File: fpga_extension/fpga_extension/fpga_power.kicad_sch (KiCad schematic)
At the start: 19 parts

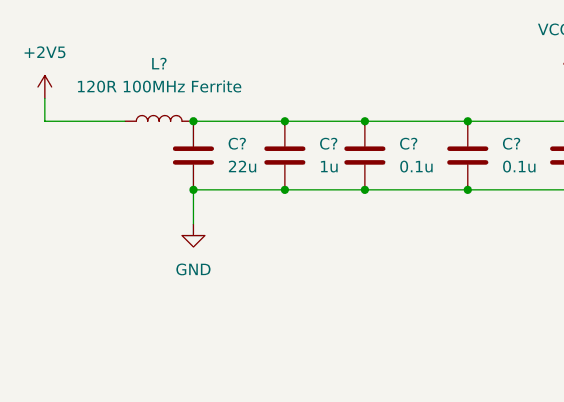
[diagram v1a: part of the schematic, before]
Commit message: gpu and motherboard passes tests, now time for fpga
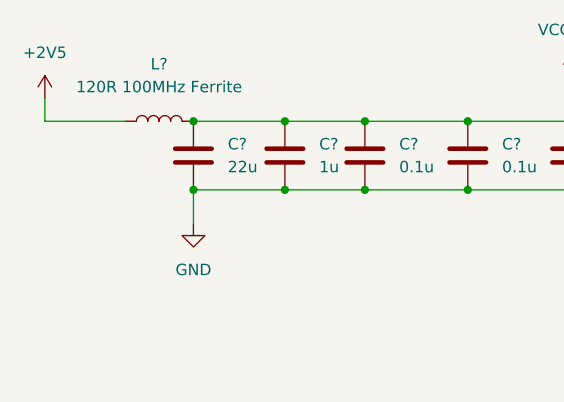
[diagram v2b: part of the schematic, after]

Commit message: refactored mainboard schematic
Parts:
- removed U?: LFE5U-25F-6BG381x, Package_BGA:Lattice_caBGA-381_17.0x17.0mm_Layout20x20_P0.8mm_Ball0.4mm_Pad0.4mm_NSMD, symbol fpga_extension_library:LFE5U-25F-6BG381x
- added U6: LFE5UM-85F-6BG381x, Package_BGA:Lattice_caBGA-381_17.0x17.0mm_Layout20x20_P0.8mm_Ball0.4mm_Pad0.4mm_NSMD, symbol FPGA_Lattice:LFE5UM-85F-6BG381x
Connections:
- new net: U6.B14 (GND), U6.B7 (GND), U6.C19 (GND), U6.D4 (GND), U6.F13 (GND), U6.F14 (GND), U6.F7 (GND), U6.F8 (GND), U6.G10 (GND), U6.G11 (GND), U6.G12 (GND), U6.G13 (GND), U6.G14 (GND), U6.G15 (GND), U6.G17 (GND), U6.G4 (GND), U6.G6 (GND), U6.G7 (GND), U6.G8 (GND), U6.G9 (GND), U6.H19 (GND), U6.J10 (GND), U6.J11 (GND), U6.J12 (GND), U6.J14 (GND), U6.J2 (GND), U6.J7 (GND), U6.J9 (GND), U6.K10 (GND), U6.K11 (GND), U6.K12 (GND), U6.K14 (GND), U6.K15 (GND), U6.K6 (GND), U6.K7 (GND), U6.K9 (GND), U6.L10 (GND), U6.L11 (GND), U6.L12 (GND), U6.L9 (GND), U6.M10 (GND), U6.M11 (GND), U6.M12 (GND), U6.M14 (GND), U6.M16 (GND), U6.M2 (GND), U6.M7 (GND), U6.M9 (GND), U6.N14 (GND), U6.N15 (GND), U6.N6 (GND), U6.N7 (GND), U6.P11 (GND), U6.P12 (GND), U6.P13 (GND), U6.P14 (GND), U6.P7 (GND), U6.P8 (GND), U6.R19 (GND), U6.U10 (GND), U6.U11 (GND), U6.U12 (GND), U6.U13 (GND), U6.U14 (GND), U6.U7 (GND), U6.U8 (GND), U6.U9 (GND), U6.V12 (GND), U6.V13 (GND), U6.V14 (GND), U6.V15 (GND), U6.V16 (GND), U6.V19 (GND), U6.V20 (GND), U6.V5 (GND), U6.V6 (GND), U6.V7 (GND), U6.V8 (GND), U6.V9 (GND), U6.W12 (GND), U6.W15 (GND), U6.W16 (GND), U6.W19 (GND), U6.W6 (GND), U6.W7 (GND)
- new net: U6.F15 (VCCAUX), U6.F6 (VCCAUX), U6.P15 (VCCAUX), U6.P6 (VCCAUX)
- new net: U6.H10 (VCC), U6.H11 (VCC), U6.H12 (VCC), U6.H13 (VCC), U6.H8 (VCC), U6.H9 (VCC), U6.J13 (VCC), U6.J8 (VCC), U6.K13 (VCC), U6.K8 (VCC), U6.L13 (VCC), U6.L8 (VCC), U6.M13 (VCC), U6.M8 (VCC), U6.N10 (VCC), U6.N11 (VCC), U6.N12 (VCC), U6.N13 (VCC), U6.N8 (VCC), U6.N9 (VCC)
- new net: U6.T15 (VCCA1), U6.U15 (VCCA1)
- new net: U6.T6 (VCCA0), U6.U6 (VCCA0)
- new net: U6.V10 (VCCAUXA0), U6.V11 (VCCAUXA0)
- new net: U6.V17 (VCCAUXA1), U6.V18 (VCCAUXA1)
